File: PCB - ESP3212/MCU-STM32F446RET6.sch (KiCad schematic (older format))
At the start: 48 parts, among them J3 20021121-00010C4LF, J4 0475890001-MicroUSBPort, P1 CONN_01X18, P2 CONN_01X18, SW1 B3U-1000P, U3 STM32F446RET6_-_TQFP64, X1 ABM3B8.000MHZB2T, X2 ABS07-32.768KHZ-9-T

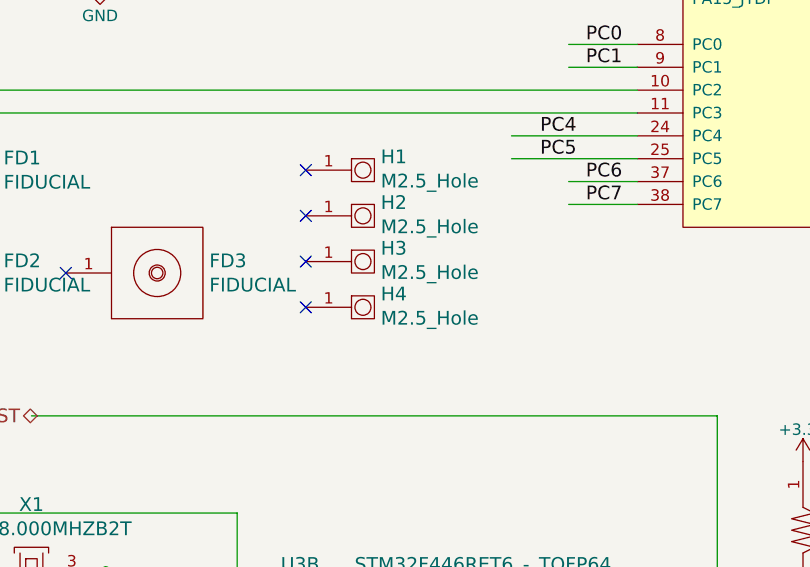
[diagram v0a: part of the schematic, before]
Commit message: Tweaks, DRC cleared, images, readme
Tweaked both designs according to the dev board scheamtics provided by
Espressif in the datasheets folder. Cleared both boards of DRC
violations, added new images and updated the readme.
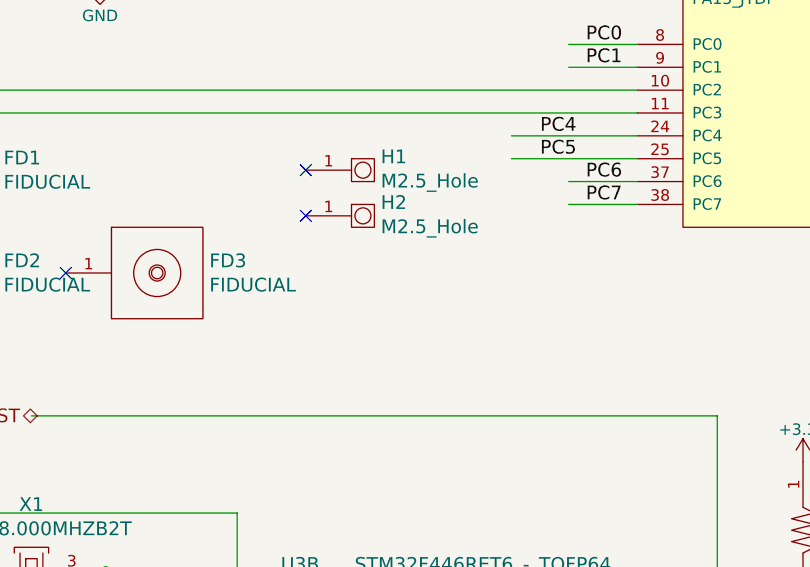
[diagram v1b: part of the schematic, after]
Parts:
- removed H3, H4: M2.5_Hole, PCB_Footprints:M2.5_HOLE, symbol M2.5_Hole
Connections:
- no-connect marks 7 -> 5
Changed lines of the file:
@@
-	1    0    0    -1
-$EndComp
-$Comp
-L M2.5_Hole H3
-U 1 1 57ED9CF6
-P 3425 4100
-F 0 "H3" H 3503 4158 60  0000 L CNN
-F 1 "M2.5_Hole" H 3503 4052 60  0000 L CNN
-F 2 "PCB_Footprints:M2.5_HOLE" H 3050 4550 197 0001 C CNN
-F 3 "" H 3425 4100 197 0001 C CNN
-	1    3425 4100
-	1    0    0    -1
-$EndComp
-$Comp
-L M2.5_Hole H4
-U 1 1 57ED9DA2
-P 3425 4300
-F 0 "H4" H 3503 4358 60  0000 L CNN
-F 1 "M2.5_Hole" H 3503 4252 60  0000 L CNN
-F 2 "PCB_Footprints:M2.5_HOLE" H 3050 4750 197 0001 C CNN
-F 3 "" H 3425 4300 197 0001 C CNN
-	1    3425 4300
 	1    0    0    -1
 $EndComp
@@
 NoConn ~ 3175 3700
 NoConn ~ 3175 3900
-NoConn ~ 3175 4100
-NoConn ~ 3175 4300
 $Comp
 L GND #PWR11
